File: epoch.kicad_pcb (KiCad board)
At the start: 2 copper layers, 28 x 34 mm, 30 parts, among them J1 USB_OTG, J2 CONN_01X05, P3 CONN_01X10, SW1 SW_Reset, SW2 SW_Up, SW3 SW_Middle, SW4 SW_Down, U1 MIC5219-3.3BM5, U2 ATSAMD21Ennc-AU, U3 DS3231MZ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

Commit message: Wire up
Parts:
- moved J2 21.6 mm to (123.8, 86.7), turned to 180 degrees
- moved C7 16.3 mm to (127.4, 73.3), turned to 90 degrees
- moved C8 13.8 mm to (127.4, 68.5), turned to 270 degrees
- moved C3 12.4 mm to (121.9, 75.6)
- moved Y1 10.9 mm to (125.3, 70.6), turned to 90 degrees
- moved C2 8.32 mm to (127.0, 65.0), turned to 0 degrees
- moved U2 3.28 mm to (118.7, 68.1), turned to 180 degrees
- moved R5 2.80 mm to (113.0, 77.2)
- moved BT1 1.63 mm to (114.6, 71.1)
- moved U4 1.05 mm to (106.7, 60.8)
- moved Y2 1.05 mm to (111.5, 62.4)
- moved P3 0.40 mm to (115.3, 82.4)
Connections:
- U2 pad 14: Net-(U2-Pad14) -> INTC
- U2 pad 25: INTC -> Net-(U2-Pad25)
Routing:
- net (+3.3): track 0.00 -> 88.7 mm, vias 0 -> 8
- net SCL: track 0.00 -> 45.2 mm
- net SDA: track 0.00 -> 43.6 mm
- net SPI_CS: track 0.00 -> 43.0 mm, vias 0 -> 2
- net SPI_SI: track 0.00 -> 41.0 mm, vias 0 -> 2
- net SPI_CLK: track 0.00 -> 38.1 mm, vias 0 -> 2
- net Net-(R5-Pad2): track 0.00 -> 34.3 mm, vias 0 -> 2
- net BUT_UP: track 0.00 -> 24.9 mm, vias 0 -> 3
- net (GND): track 0.00 -> 21.3 mm, vias 0 -> 8
- net SWDIO: track 0.00 -> 20.1 mm
- net VCC: track 0.00 -> 17.2 mm, vias 0 -> 2
- net BUT_MID: track 0.00 -> 15.8 mm, vias 0 -> 1
- net BUT_DWN: track 0.00 -> 15.6 mm, vias 0 -> 1
- net SWDCLK: track 0.00 -> 14.3 mm
- net EXTMODE: track 0.00 -> 10.6 mm
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- added copper zone on B.Cu, net (GND)
- added copper zone on F.Cu, net (GND)
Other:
- outline, holes or cut-outs redrawn
- board text added: "+3.3V"
- board text added: "GND"
- board text added: "RST"
- board text added: "SCLK"
- board text added: "SDIO"

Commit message: Update resonator crystal to 18pF and create BOM csv
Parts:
- C7, C8: value 4.7pF -> 18pF
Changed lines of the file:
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@@
       (effects (font (size 1 1) (thickness 0.15)))
     )
-    (fp_text value 4.7pF (at -1.016 17.907 90) (layer F.Fab)
+    (fp_text value 18pF (at -1.016 17.907 90) (layer F.Fab)
       (effects (font (size 1 1) (thickness 0.15)))
     )
@@
       (effects (font (size 1 1) (thickness 0.15)))
     )
-    (fp_text value 4.7pF (at 1.397 -10.922 270) (layer F.Fab)
+    (fp_text value 18pF (at 1.397 -10.922 270) (layer F.Fab)
       (effects (font (size 1 1) (thickness 0.15)))
     )

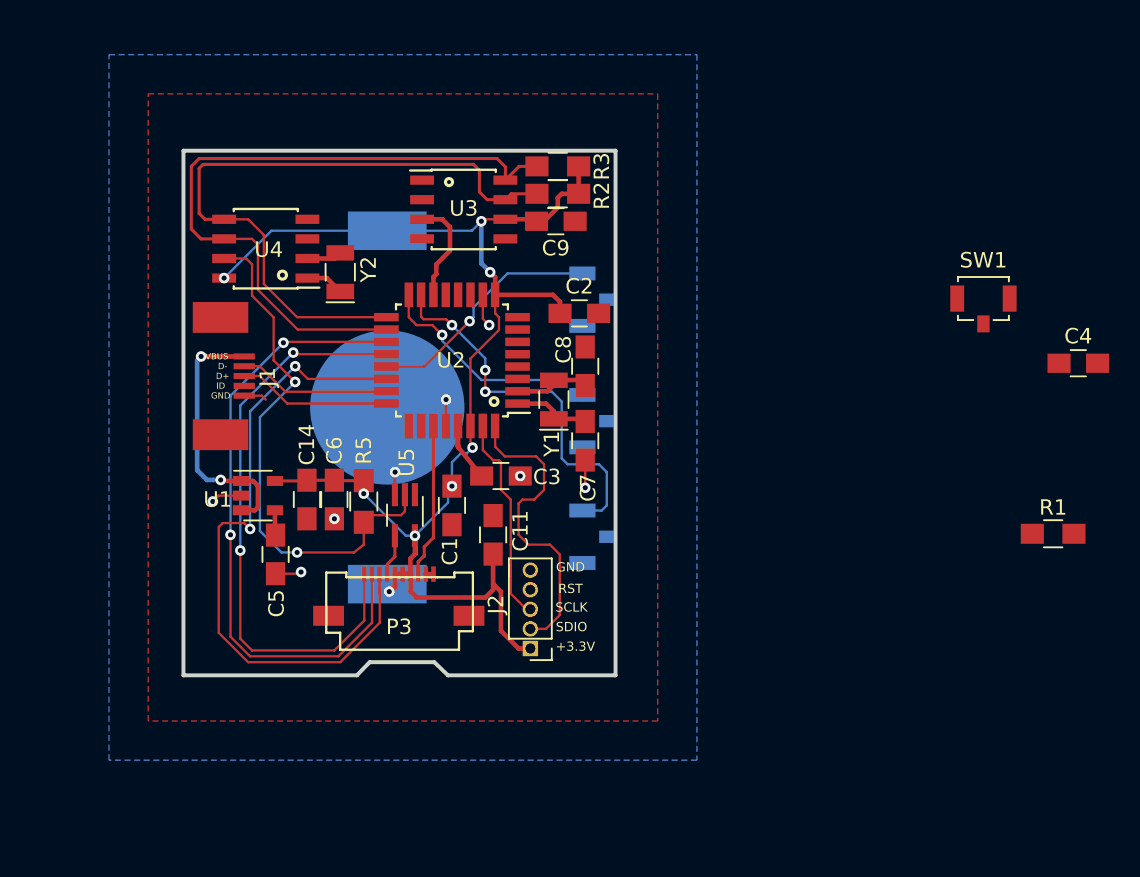
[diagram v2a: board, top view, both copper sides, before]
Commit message: Place drill holes.
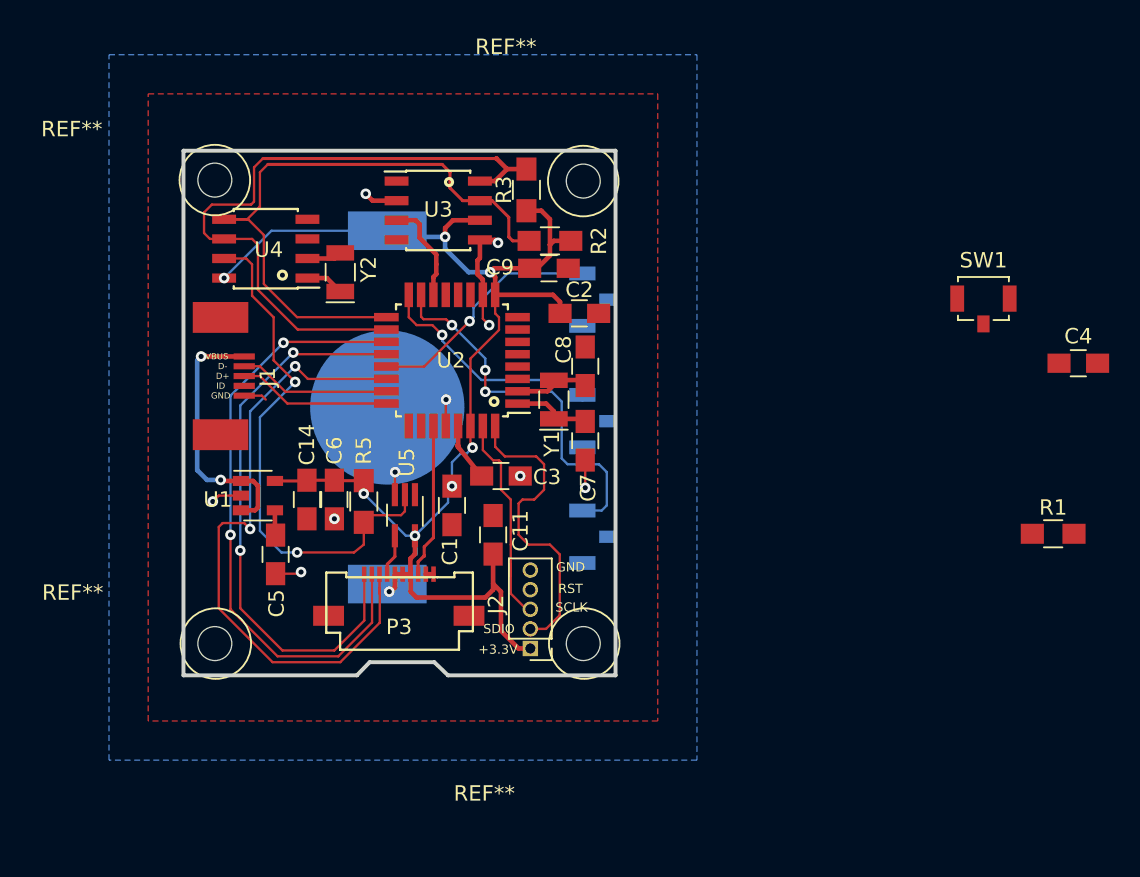
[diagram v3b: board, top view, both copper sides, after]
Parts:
- added REF**: 1pin, Connectors:1pin, F.Cu at (127.3, 56.5)
- added REF**: 1pin, Connectors:1pin, F.Cu at (127.3, 86.4)
- added REF**: 1pin, Connectors:1pin, F.Cu at (103.4, 86.4)
- added REF**: 1pin, Connectors:1pin, F.Cu at (103.4, 56.4)
- moved R2 3.09 mm to (125.1, 60.3)
- moved C9 3.08 mm to (125.0, 62.1)
- moved R3 2.54 mm to (123.6, 57.0), turned to 90 degrees
- moved U3 1.65 mm to (117.9, 58.4)
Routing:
- net (GND): track 21.3 -> 28.5 mm, vias 8 -> 10
- net SDA: track 43.6 -> 40.9 mm
- net (+3.3): track 88.7 -> 90.7 mm
- net SCL: track 45.2 -> 43.5 mm
- net SPI_CLK: track 38.1 -> 37.0 mm
- net SPI_SI: track 41.0 -> 39.9 mm
- net SPI_CS: track 43.0 -> 42.0 mm

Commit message: Round corners and add LED
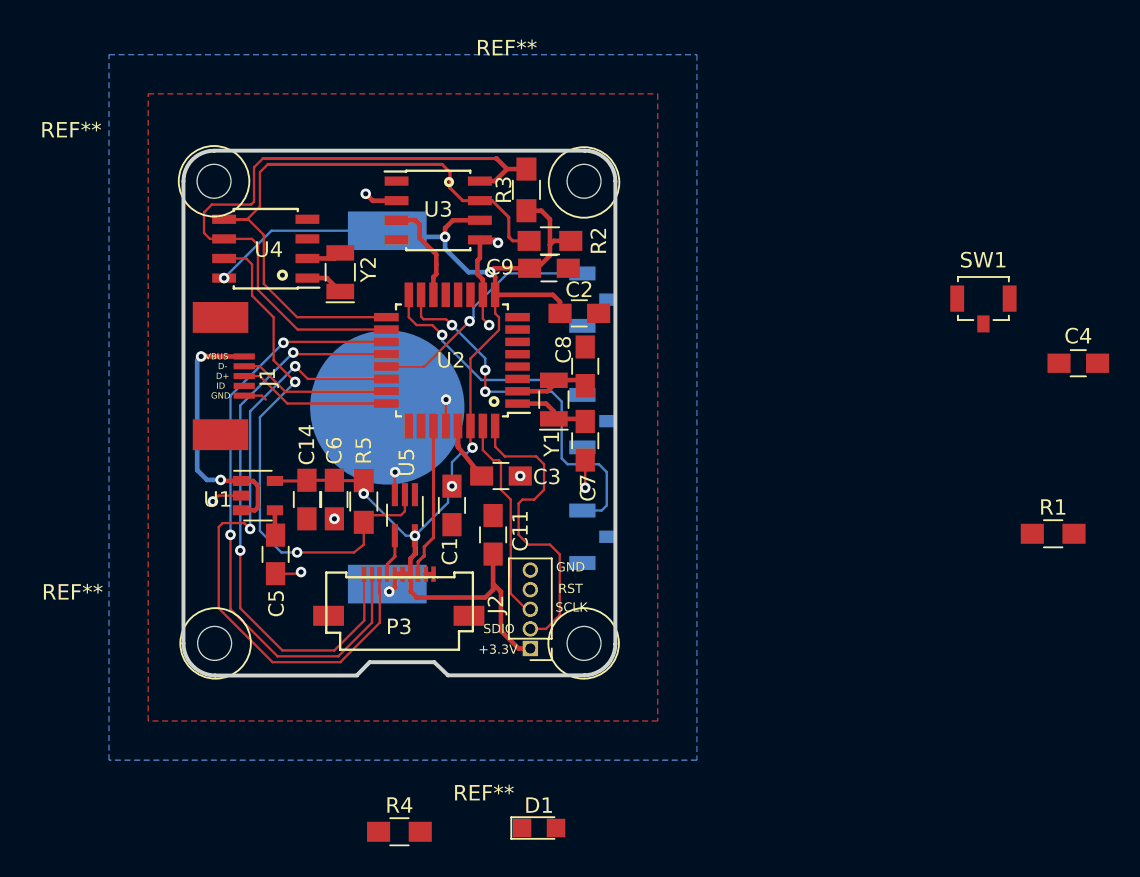
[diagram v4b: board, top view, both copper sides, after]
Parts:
- added D1: LED, LEDs:LED_0805, F.Cu at (124.4, 98.4)
- added R4: 499, Resistors_SMD:R_0805_HandSoldering, F.Cu at (115.3, 98.6)
- moved REF** 0.10 mm to (127.3, 56.5)
- moved REF** 0.09 mm to (103.3, 56.5)
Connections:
- U2 pad 7: Net-(U2-Pad7) -> LED
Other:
- outline, holes or cut-outs redrawn

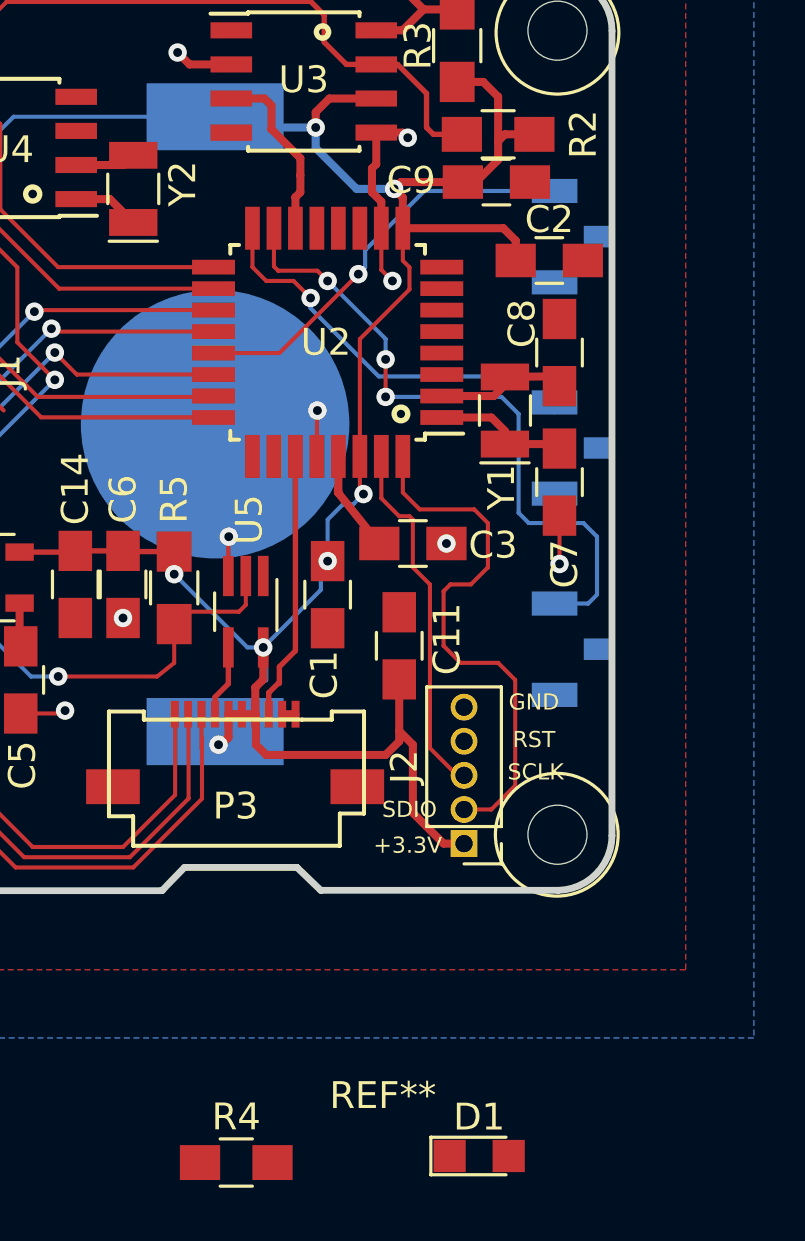
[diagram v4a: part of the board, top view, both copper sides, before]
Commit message: Route LED
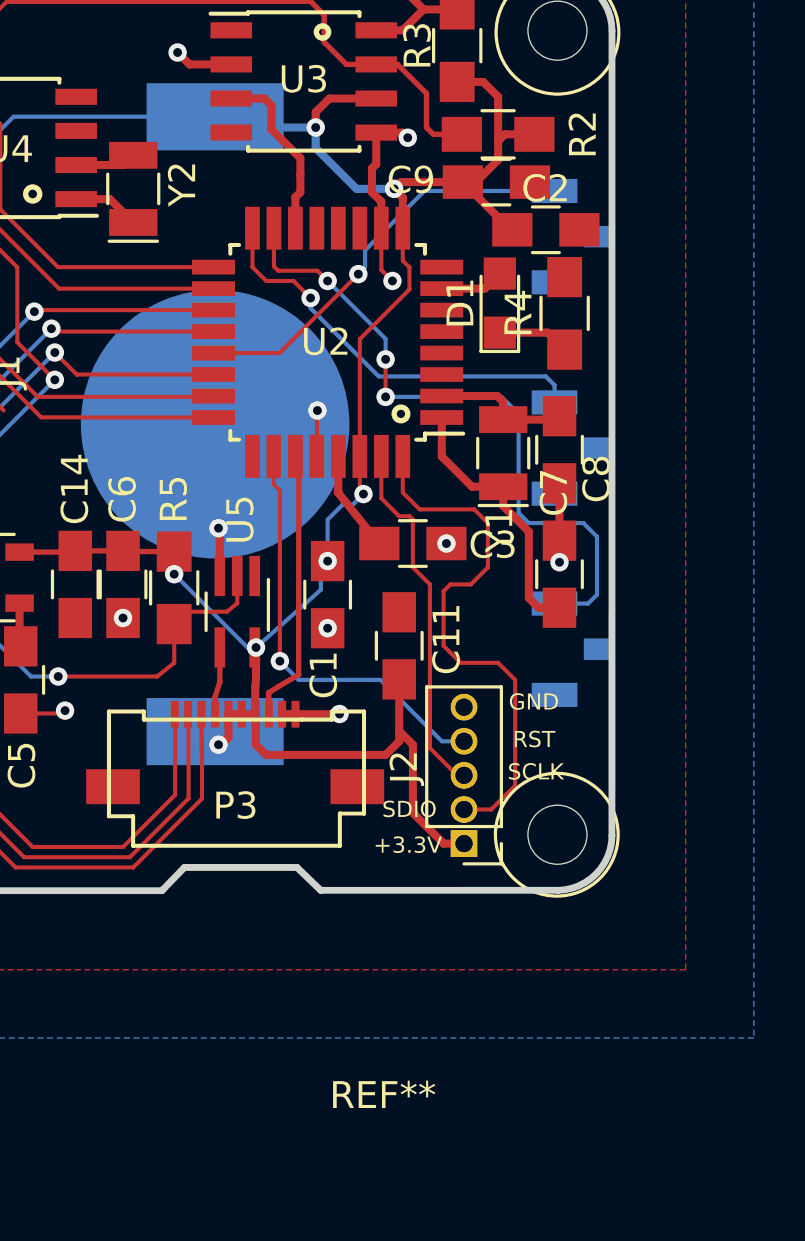
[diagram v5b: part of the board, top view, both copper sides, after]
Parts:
- moved R4 33.9 mm to (127.6, 67.0), turned to 90 degrees
- moved D1 31.8 mm to (125.2, 66.6), turned to 90 degrees
- moved C8 3.62 mm to (127.4, 72.1), turned to 90 degrees
- moved C7 3.43 mm to (127.4, 76.7), turned to 270 degrees
- moved Y1 1.59 mm to (125.3, 72.2)
- moved C2 1.15 mm to (126.9, 63.9)
- moved U5 0.32 mm to (115.4, 78.1)
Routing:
- net RESET: track 0.00 -> 15.8 mm, vias 0 -> 1
- net (GND): track 28.5 -> 35.1 mm, vias 10 -> 12
- net Net-(C7-Pad2): track 5.15 -> 10.1 mm
- net (+3.3): track 90.7 -> 87.3 mm
- net Net-(D1-Pad1): track 0.00 -> 2.67 mm
- net LED: track 0.00 -> 2.40 mm
- net Net-(C8-Pad2): track 4.97 -> 5.73 mm
